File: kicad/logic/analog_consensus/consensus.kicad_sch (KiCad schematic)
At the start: 8 parts, among them Q1 BSS8402DW-7-F, Q2 BSS8402DW-7-F

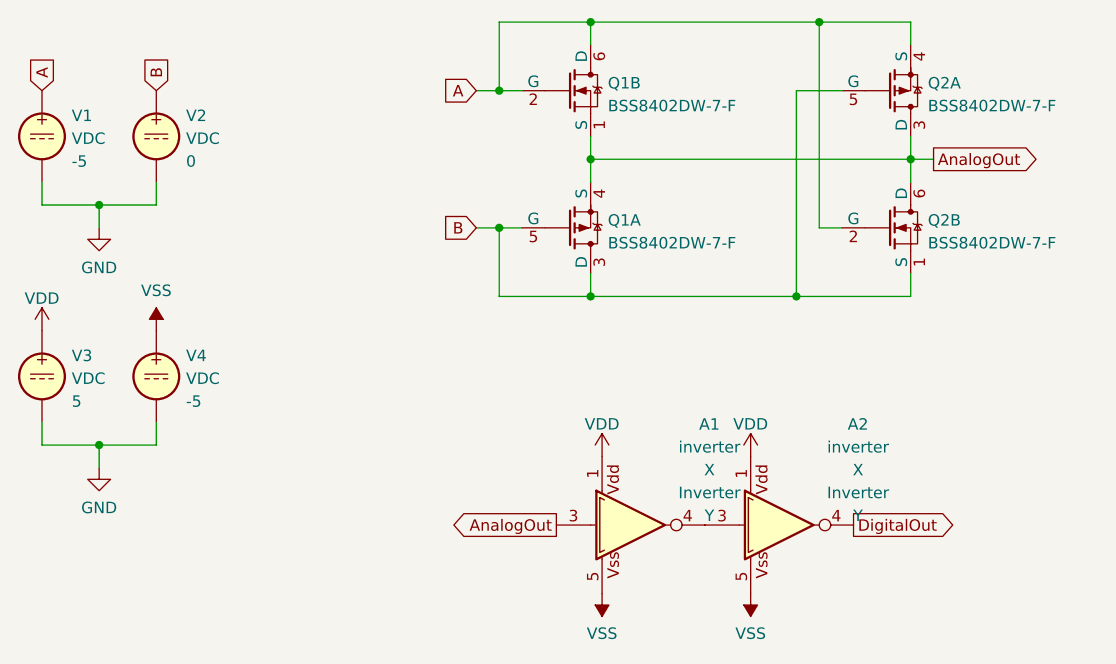
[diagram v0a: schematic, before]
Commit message: update to kicad 9
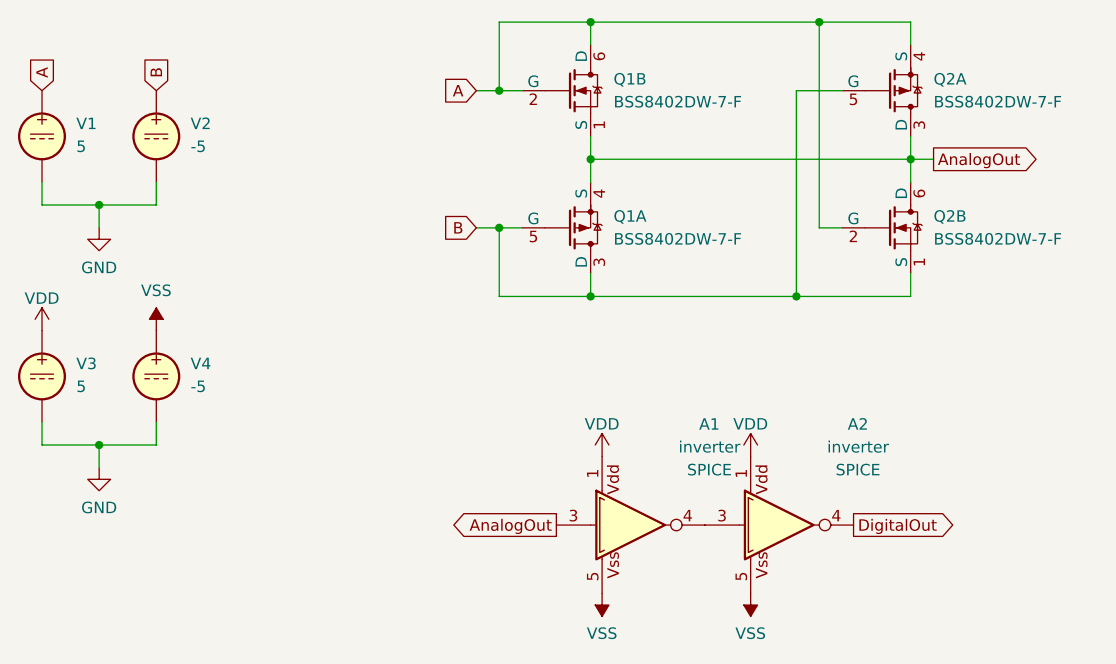
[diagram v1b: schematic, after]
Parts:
- A1, A2: Spice_Lib_File ${TRITIUM_LIB}/TritiumSpice.lib -> (none); Spice_Model Inverter -> (none); Spice_Netlist_Enabled Y -> (none); Spice_Primitive X -> (none)
- Q1, Q2: Spice_Lib_File ${TRITIUM_LIB}/TritiumSpice.lib -> (none); Spice_Model BSS8402DW -> (none); Spice_Primitive X -> (none)
- V1: value VDC -> 5; Spice_Model -5 -> (none); Spice_Netlist_Enabled Y -> (none); Spice_Primitive V -> (none)
- V2: value VDC -> -5; Spice_Model 0 -> (none); Spice_Netlist_Enabled Y -> (none); Spice_Primitive V -> (none)
- V3: value VDC -> 5; Spice_Model 5 -> (none); Spice_Netlist_Enabled Y -> (none); Spice_Primitive V -> (none)
- V4: value VDC -> -5; Spice_Model -5 -> (none); Spice_Netlist_Enabled Y -> (none); Spice_Primitive V -> (none)
